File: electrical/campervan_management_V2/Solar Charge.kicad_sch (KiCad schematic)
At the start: 12 parts, among them Q1 MDD2302, Q2 MDD2302, U3 LTV-817S-TA1-C, U8 LTV-817S-TA1-C

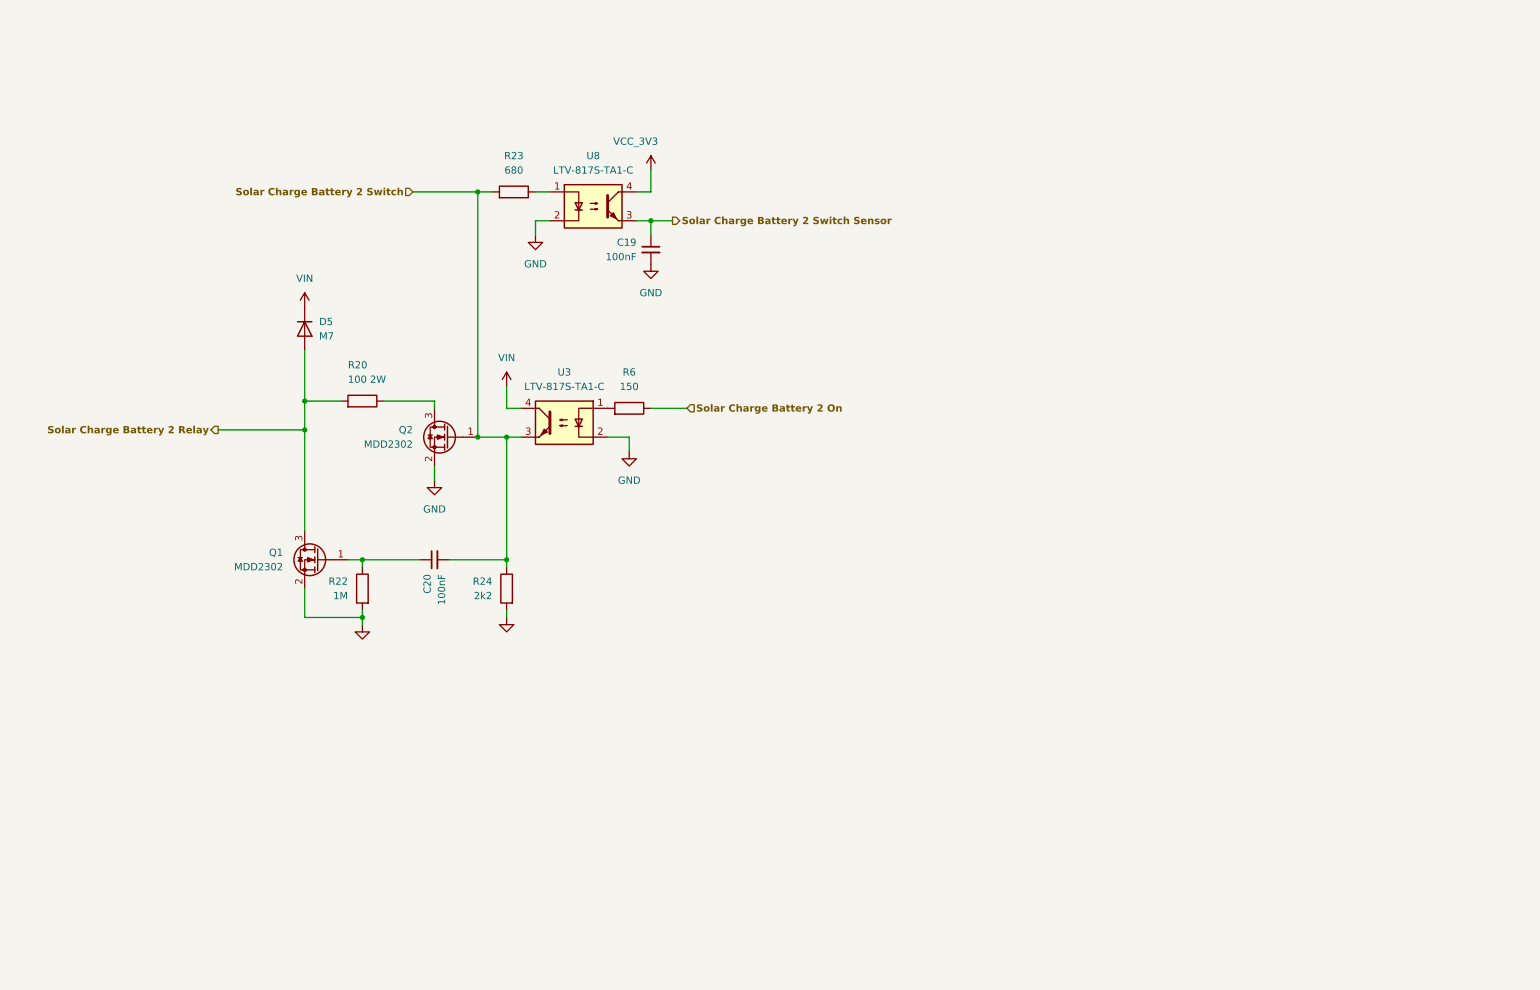
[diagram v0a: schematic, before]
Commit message: Changed to high side relay drive and added 4.1V PS for high side relay hold
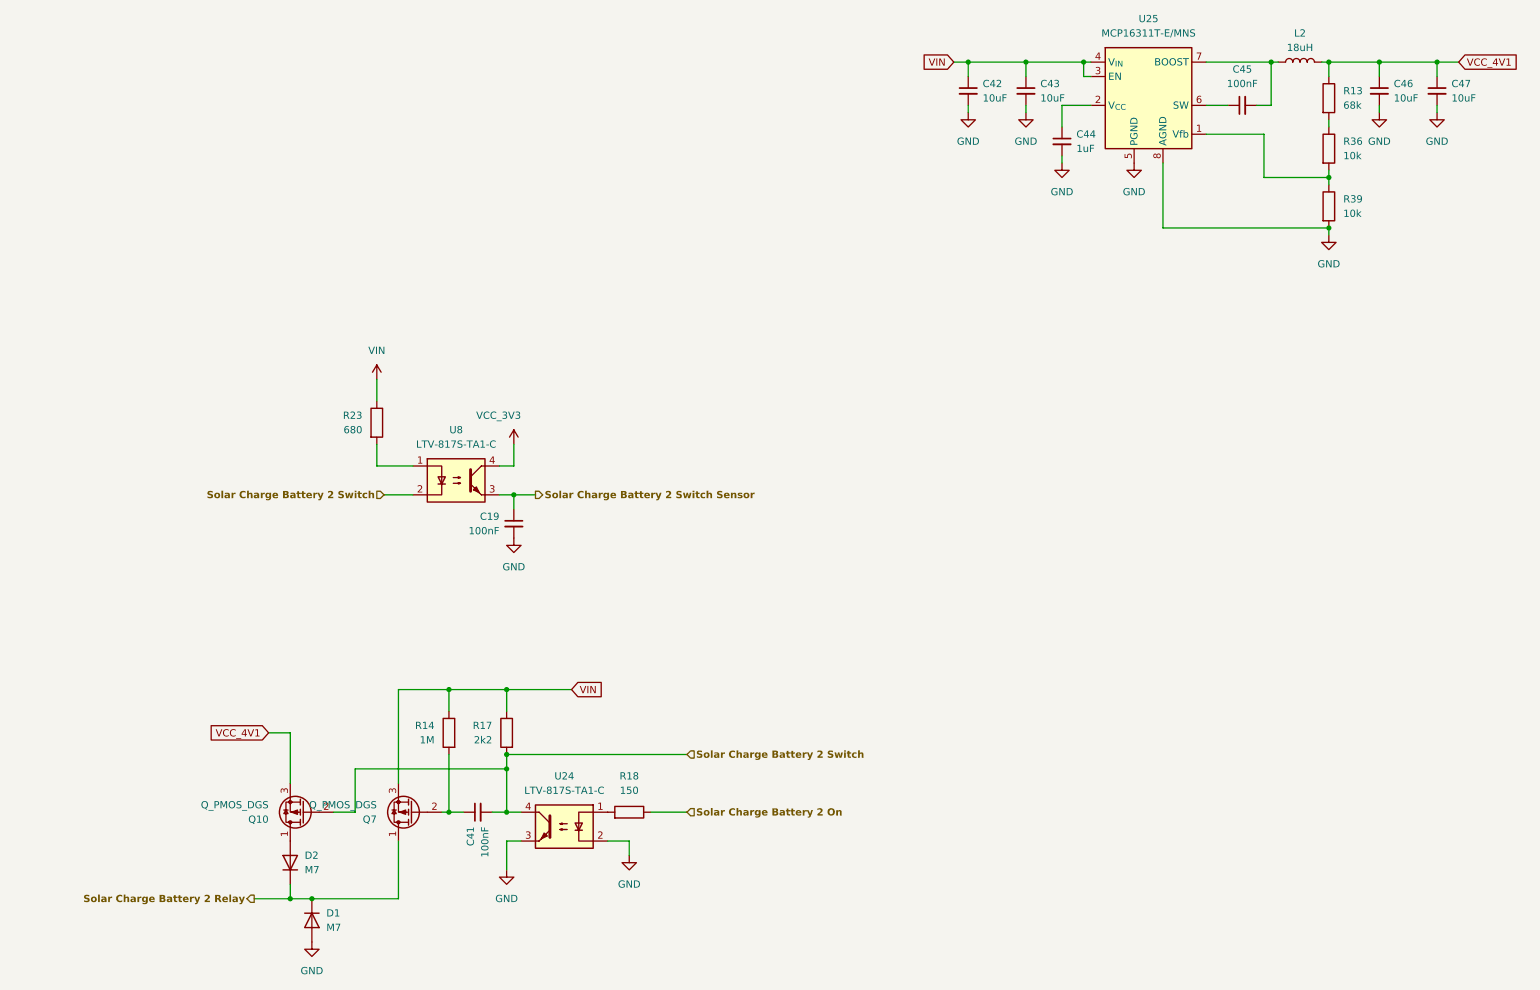
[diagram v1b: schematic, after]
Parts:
- removed C20: 100nF, Capacitor_SMD:C_0805_2012Metric, symbol Device:C_Small
- removed D5: M7, Diode_SMD:D_SMA, symbol Diode:1N4001
- removed Q1, Q2: MDD2302, Package_TO_SOT_SMD:SOT-23, symbol camper_van:MDD2302
- removed R20: 100 2W, Resistor_SMD:R_2512_6332Metric, symbol Device:R
- removed R22: 1M, Resistor_SMD:R_0805_2012Metric, symbol Device:R
- removed R24: 2k2, Resistor_SMD:R_0805_2012Metric, symbol Device:R
- removed R6: 150, Resistor_SMD:R_0805_2012Metric, symbol Device:R
- removed U3: LTV-817S-TA1-C, Package_SO:SO-4_4.4x3.6mm_P2.54mm, symbol Isolator:LTV-357T
- added C41: 100nF, Capacitor_SMD:C_0805_2012Metric, symbol Device:C_Small
- added C42, C43, C46, C47: 10uF, Capacitor_SMD:C_1206_3216Metric, symbol camper_van:C_SMD_Ceramic_0805
- added C44: 1uF, Capacitor_SMD:C_0805_2012Metric, symbol Device:C_Small
- added C45: 100nF, Capacitor_SMD:C_0805_2012Metric, symbol camper_van:C_SMD_Ceramic_0402
- added D1, D2: M7, Diode_SMD:D_SMA, symbol Diode:1N4001
- added L2: 18uH, Inductor_SMD:L_Coilcraft_MSS1038-XXX, symbol Device:L
- added Q10, Q7: Q_PMOS_DGS, Package_TO_SOT_SMD:SOT-23, symbol Transistor_FET:Q_PMOS_DGS
- added R13: 68k, Resistor_SMD:R_0805_2012Metric, symbol Device:R
- added R14: 1M, Resistor_SMD:R_0805_2012Metric, symbol Device:R
- added R17: 2k2, Resistor_SMD:R_0805_2012Metric, symbol Device:R
- added R18: 150, Resistor_SMD:R_0805_2012Metric, symbol Device:R
- added R36, R39: 10k, Resistor_SMD:R_0603_1608Metric, symbol Device:R
- added U24: LTV-817S-TA1-C, Package_SO:SO-4_4.4x3.6mm_P2.54mm, symbol Isolator:LTV-357T
- added U25: MCP16311T-E/MNS, Package_SO:MSOP-8_3x3mm_P0.65mm, symbol camper_van:MCP16311x-xMNY
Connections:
- net GND: now also C42.2, C43.2, C44.2, C46.2, C47.2, D1.2 (A), R39.2, U24.2, U24.3, U25.5 (PGND), U25.8 (AGND); no longer U8.2
- net Solar Charge Battery 2 On: now also R18.1
- net Solar Charge Battery 2 Relay: now also D1.1 (K), D2.1 (K), Q7.1 (D)
- net Solar Charge Battery 2 Switch: now also U8.2, C41.2, Q10.2 (G), R17.2, U24.4; no longer R23.2
- net VIN: now also R23.1, C42.1, C43.1, Q7.3 (S), R14.1, R17.1, U25.3 (EN), U25.4 (V_{IN})
- net at U8.1: now also R23.2; no longer R23.1
- new net: D2.2 (A), Q10.1 (D)
- new net: R13.2, R36.1
- new net: C41.1, Q7.2 (G), R14.2
- new net: C44.1, U25.2 (V_{CC})
- new net: R36.2, R39.1, U25.1 (Vfb)
- new net: C45.1, U25.6 (SW)
- new net: C45.2, L2.1, U25.7 (BOOST)
- new net: R18.2, U24.1
- new net VCC_4V1: C46.1, C47.1, L2.2, Q10.3 (S), R13.1
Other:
- moved on the sheet: C19, R23, U8

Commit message: updated
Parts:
- R13: footprint Resistor_SMD:R_0805_2012Metric -> Resistor_SMD:R_0603_1608Metric; Extended B -> (none); LCSC PN C17801 -> (none)
- R17: value 2k2 -> 47k
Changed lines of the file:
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@@
 			)
 		)
-		(property "Footprint" "Resistor_SMD:R_0805_2012Metric"
+		(property "Footprint" "Resistor_SMD:R_0603_1608Metric"
 			(at 245.872 31.75 90)
 			(effects
@@
 			)
 		)
-		(property "LCSC PN" "C17801"
+		(property "LCSC PN" ""
 			(at 247.65 31.75 0)
 			(effects
@@
 			)
 		)
-		(property "Extended" "B"
+		(property "Extended" ""
 			(at 247.65 31.75 0)
 			(effects
@@
 			)
 		)
-		(property "Value" "2k2"
+		(property "Value" "47k"
 			(at 100.33 144.7799 0)
 			(effects

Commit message: First attempt at PCB layout
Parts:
- C13: renamed from C44; footprint Capacitor_SMD:C_0805_2012Metric -> Capacitor_SMD:C_0603_1608Metric; LCSC PN C28323 -> C15849
- U3: renamed from U25; value MCP16311T-E/MNS -> MCP16311x-xMNY; footprint Package_SO:MSOP-8_3x3mm_P0.65mm -> Package_DFN_QFN:DFN-8-1EP_3x2mm_P0.5mm_EP1.75x1.45mm; Extended E -> (none); LCSC PN C627024 -> (none)
- renumbered C45 to C15, C42 to C16, C43 to C17, C47 to C18, C46 to C19, C41 to C29, C19 to C34, D1 to D3, D2 to D4, Q7 to Q5, Q10 to Q6, R23 to R13, R14 to R28, R17 to R29, R18 to R34, R13 to R5, R36 to R6, R39 to R7, U24 to U16, U8 to U7
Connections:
- net GND: now also U3.9 (GND)
- net at U3.6 (SW): now also C15.2, L2.1; no longer C15.1
- new net: C15.1, U3.7 (BOOST)
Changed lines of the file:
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@@
 		(dnp no)
 		(fields_autoplaced yes)
-		(property "Reference" "C46"
+		(property "Reference" "C19"
 			(at 259.08 29.2162 0)
 			(effects
@@
 			(project "campervan_management_V2"
 				(path "/870a08cc-a6e6-4310-b4b3-ae6af01530aa/d660ade9-7cc1-406f-a2c6-d65746f825ab"
-					(reference "C46")
+					(reference "C19")
 					(unit 1)
 				)
@@
 		(dnp no)
 		(fields_autoplaced yes)
-		(property "Reference" "D2"
+		(property "Reference" "D4"
 			(at 67.31 165.0999 90)
 			(effects
@@
 			(project "campervan_management_V2"
 				(path "/870a08cc-a6e6-4310-b4b3-ae6af01530aa/d660ade9-7cc1-406f-a2c6-d65746f825ab"
-					(reference "D2")
+					(reference "D4")
 					(unit 1)
 				)
@@
 		(dnp no)
 		(fields_autoplaced yes)
-		(property "Reference" "R13"
+		(property "Reference" "R5"
 			(at 250.19 30.4799 0)
 			(effects
@@
 			(project "campervan_management_V2"
 				(path "/870a08cc-a6e6-4310-b4b3-ae6af01530aa/d660ade9-7cc1-406f-a2c6-d65746f825ab"
-					(reference "R13")
+					(reference "R5")
 					(unit 1)
 				)
@@
 		(on_board yes)
 		(dnp no)
-		(property "Reference" "Q7"
+		(property "Reference" "Q5"
 			(at 80.01 158.7501 0)
 			(effects
@@
 			(project "campervan_management_V2"
 				(path "/870a08cc-a6e6-4310-b4b3-ae6af01530aa/d660ade9-7cc1-406f-a2c6-d65746f825ab"
-					(reference "Q7")
+					(reference "Q5")
 					(unit 1)
 				)
@@
 		(on_board yes)
 		(dnp no)
-		(property "Reference" "U8"
+		(property "Reference" "U7"
 			(at 93.98 90.17 0)
 			(effects
@@
 			(project "campervan_management_V2"
 				(path "/870a08cc-a6e6-4310-b4b3-ae6af01530aa/d660ade9-7cc1-406f-a2c6-d65746f825ab"
-					(reference "U8")
+					(reference "U7")
 					(unit 1)
 				)
@@
 		(dnp no)
 		(fields_autoplaced yes)
-		(property "Reference" "C43"
+		(property "Reference" "C17"
 			(at 196.85 29.2162 0)
 			(effects
@@
 			(project "campervan_management_V2"
 				(path "/870a08cc-a6e6-4310-b4b3-ae6af01530aa/d660ade9-7cc1-406f-a2c6-d65746f825ab"
-					(reference "C43")
+					(reference "C17")
 					(unit 1)
 				)
@@
 		(dnp no)
 		(fields_autoplaced yes)
-		(property "Reference" "C44"
+		(property "Reference" "C13"
 			(at 203.2 38.1062 0)
 			(effects
@@
 			)
 		)
-		(property "Footprint" "Capacitor_SMD:C_0805_2012Metric"
+		(property "Footprint" "Capacitor_SMD:C_0603_1608Metric"
 			(at 200.66 39.37 0)
 			(effects
@@
 			)
 		)
-		(property "LCSC PN" "C28323"
+		(property "LCSC PN" "C15849"
 			(at 200.66 39.37 0)
 			(effects
@@
 			(project "campervan_management_V2"
 				(path "/870a08cc-a6e6-4310-b4b3-ae6af01530aa/d660ade9-7cc1-406f-a2c6-d65746f825ab"
-					(reference "C44")
+					(reference "C13")
 					(unit 1)
 				)
@@
 		(dnp no)
 		(fields_autoplaced yes)
-		(property "Reference" "U25"
+		(property "Reference" "U3"
 			(at 215.9 17.78 0)
 			(effects
@@
 			)
 		)
-		(property "Value" "MCP16311T-E/MNS"
+		(property "Value" "MCP16311x-xMNY"
 			(at 215.9 20.32 0)
 			(effects
@@
 			)
 		)
-		(property "Footprint" "Package_SO:MSOP-8_3x3mm_P0.65mm"
+		(property "Footprint" "Package_DFN_QFN:DFN-8-1EP_3x2mm_P0.5mm_EP1.75x1.45mm"
 			(at 217.17 39.37 0)
 			(effects
@@
 			)
 		)
-		(property "LCSC PN" "C627024"
-			(at 215.9 30.48 0)
-			(effects
-				(font
-					(size 1.27 1.27)
-				)
-				(hide yes)
-			)
-		)
-		(property "Extended" "E"
-			(at 215.9 30.48 0)
-			(effects
-				(font
-					(size 1.27 1.27)
-				)
-				(hide yes)
-			)
-		)
 		(pin "8"
 		)
@@
 		(pin "3"
 		)
-		(instances
-			(project "campervan_management_V2"
-				(path "/870a08cc-a6e6-4310-b4b3-ae6af01530aa/d660ade9-7cc1-406f-a2c6-d65746f825ab"
-					(reference "U25")
+		(pin "9"
+		)
+		(instances
+			(project "campervan_management_V2"
+				(path "/870a08cc-a6e6-4310-b4b3-ae6af01530aa/d660ade9-7cc1-406f-a2c6-d65746f825ab"
+					(reference "U3")
 					(unit 1)
 				)
@@
 		(dnp no)
 		(fields_autoplaced yes)
-		(property "Reference" "D1"
+		(property "Reference" "D3"
 			(at 71.12 175.2599 90)
 			(effects
@@
 			(project "campervan_management_V2"
 				(path "/870a08cc-a6e6-4310-b4b3-ae6af01530aa/d660ade9-7cc1-406f-a2c6-d65746f825ab"
-					(reference "D1")
+					(reference "D3")
 					(unit 1)
 				)
@@
 		(dnp no)
 		(fields_autoplaced yes)
-		(property "Reference" "C42"
+		(property "Reference" "C16"
 			(at 186.69 29.2162 0)
 			(effects
@@
 			(project "campervan_management_V2"
 				(path "/870a08cc-a6e6-4310-b4b3-ae6af01530aa/d660ade9-7cc1-406f-a2c6-d65746f825ab"
-					(reference "C42")
+					(reference "C16")
 					(unit 1)
 				)
@@
 		(dnp no)
 		(fields_autoplaced yes)
-		(property "Reference" "R18"
+		(property "Reference" "R34"
 			(at 124.46 151.13 90)
 			(effects
@@
 			(project "campervan_management_V2"
 				(path "/870a08cc-a6e6-4310-b4b3-ae6af01530aa/d660ade9-7cc1-406f-a2c6-d65746f825ab"
-					(reference "R18")
+					(reference "R34")
 					(unit 1)
 				)
@@
 		(on_board yes)
 		(dnp no)
-		(property "Reference" "R23"
+		(property "Reference" "R13"
 			(at 77.47 87.6299 0)
 			(effects
@@
 			(project "campervan_management_V2"
 				(path "/870a08cc-a6e6-4310-b4b3-ae6af01530aa/d660ade9-7cc1-406f-a2c6-d65746f825ab"
-					(reference "R23")
+					(reference "R13")
 					(unit 1)
 				)
@@
 		(dnp no)
 		(fields_autoplaced yes)
-		(property "Reference" "R14"
+		(property "Reference" "R28"
 			(at 90.17 142.2399 0)
 			(effects
@@
 			(project "campervan_management_V2"
 				(path "/870a08cc-a6e6-4310-b4b3-ae6af01530aa/d660ade9-7cc1-406f-a2c6-d65746f825ab"
-					(reference "R14")
+					(reference "R28")
 					(unit 1)
 				)
@@
 		(on_board yes)
 		(dnp no)
-		(property "Reference" "U24"
+		(property "Reference" "U16"
 			(at 113.03 151.13 0)
 			(effects
@@
 			(project "campervan_management_V2"
 				(path "/870a08cc-a6e6-4310-b4b3-ae6af01530aa/d660ade9-7cc1-406f-a2c6-d65746f825ab"
-					(reference "U24")
+					(reference "U16")
 					(unit 1)
 				)
@@
 		(dnp no)
 		(fields_autoplaced yes)
-		(property "Reference" "R39"
+		(property "Reference" "R7"
 			(at 250.19 49.5299 0)
 			(effects
@@
 			(project "campervan_management_V2"
 				(path "/870a08cc-a6e6-4310-b4b3-ae6af01530aa/d660ade9-7cc1-406f-a2c6-d65746f825ab"
-					(reference "R39")
+					(reference "R7")
 					(unit 1)
 				)
@@
 		(on_board yes)
 		(dnp no)
-		(property "Reference" "Q10"
+		(property "Reference" "Q6"
 			(at 60.96 158.7501 0)
 			(effects
@@
 			(project "campervan_management_V2"
 				(path "/870a08cc-a6e6-4310-b4b3-ae6af01530aa/d660ade9-7cc1-406f-a2c6-d65746f825ab"
-					(reference "Q10")
+					(reference "Q6")
 					(unit 1)
 				)
@@
 		(on_board yes)
 		(dnp no)
-		(property "Reference" "C19"
+		(property "Reference" "C34"
 			(at 101.6 105.4162 0)
 			(effects
@@
 			(project "campervan_management_V2"
 				(path "/870a08cc-a6e6-4310-b4b3-ae6af01530aa/d660ade9-7cc1-406f-a2c6-d65746f825ab"
-					(reference "C19")
+					(reference "C34")
 					(unit 1)
 				)
@@
 		(dnp no)
 		(fields_autoplaced yes)
-		(property "Reference" "C47"
+		(property "Reference" "C18"
 			(at 269.24 29.2162 0)
 			(effects
@@
 			(project "campervan_management_V2"
 				(path "/870a08cc-a6e6-4310-b4b3-ae6af01530aa/d660ade9-7cc1-406f-a2c6-d65746f825ab"
-					(reference "C47")
+					(reference "C18")
 					(unit 1)
 				)
@@
 		(on_board yes)
 		(dnp no)
-		(property "Reference" "R17"
+		(property "Reference" "R29"
 			(at 100.33 142.2399 0)
 			(effects
@@
 			(project "campervan_management_V2"
 				(path "/870a08cc-a6e6-4310-b4b3-ae6af01530aa/d660ade9-7cc1-406f-a2c6-d65746f825ab"
-					(reference "R17")
+					(reference "R29")
 					(unit 1)
 				)
@@
 		(on_board yes)
 		(dnp no)
-		(property "Reference" "C41"
+		(property "Reference" "C29"
 			(at 96.5262 160.02 0)
 			(effects
@@
 			(project "campervan_management_V2"
 				(path "/870a08cc-a6e6-4310-b4b3-ae6af01530aa/d660ade9-7cc1-406f-a2c6-d65746f825ab"
-					(reference "C41")
+					(reference "C29")
 					(unit 1)
 				)
@@
 		(dnp no)
 		(fields_autoplaced yes)
-		(property "Reference" "C45"
+		(property "Reference" "C15"
 			(at 232.4163 26.67 90)
 			(effects
@@
 			(project "campervan_management_V2"
 				(path "/870a08cc-a6e6-4310-b4b3-ae6af01530aa/d660ade9-7cc1-406f-a2c6-d65746f825ab"
-					(reference "C45")
+					(reference "C15")
 					(unit 1)
 				)
@@
 		(dnp no)
 		(fields_autoplaced yes)
-		(property "Reference" "R36"
+		(property "Reference" "R6"
 			(at 250.19 39.3699 0)
 			(effects
@@
 			(project "campervan_management_V2"
 				(path "/870a08cc-a6e6-4310-b4b3-ae6af01530aa/d660ade9-7cc1-406f-a2c6-d65746f825ab"
-					(reference "R36")
-					(unit 1)
-				)
+					(reference "R6")
+					(unit 1)
+				)

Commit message: Close to final design
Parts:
- removed Q5, Q6: Q_PMOS_DGS, Package_TO_SOT_SMD:SOT-23, symbol Transistor_FET:Q_PMOS_DGS
- added Q3, Q4: FDS4685, Package_SO:SOIC-8_3.9x4.9mm_P1.27mm, symbol Transistor_FET:FDS9435A
- L1: renamed from L2; Extended E -> (none); LCSC PN C19191679 -> (none)
- R1: renamed from R5; Extended (none) -> B; LCSC PN (none) -> C23231
- R13: renamed from R29; LCSC PN C17520 -> C17713
- U1: renamed from U3; Extended (none) -> E; JLCPCB (none) -> 1.05; LCSC PN (none) -> C510882; e14 (none) -> 3.55
- renumbered C13 to C1, C18 to C10, C29 to C16, C15 to C2, C34 to C21, C16 to C5, C17 to C6, C19 to C9, D4 to D5, R28 to R10, R13 to R15, R6 to R2, R34 to R25, R7 to R4, U16 to U12
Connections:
- net Solar Charge Battery 2 Relay: now also Q3.5 (D), Q3.6 (D), Q3.7 (D), Q3.8 (D)
- net Solar Charge Battery 2 Switch: now also Q4.4 (G)
- net VCC_4V1: now also Q4.1 (S), Q4.2 (S), Q4.3 (S)
- net VIN: now also Q3.1 (S), Q3.2 (S), Q3.3 (S)
- net test: now reaches D5.2 (A)
- net test: now also Q4.5 (D), Q4.6 (D), Q4.7 (D), Q4.8 (D)
- net at C16.1, R10.2: now also Q3.4 (G)
- net Net-(R16-Pad2): now reaches R15.2, U7.1
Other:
- moved on the sheet: R25, U12
